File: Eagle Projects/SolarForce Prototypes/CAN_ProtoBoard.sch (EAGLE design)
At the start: 18 parts, among them U1 MCP2551

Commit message: CAN ProtoPCB V1 Ready..
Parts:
- added !INT, CLKOUT, RX, RX0BF, RX1BF, TX, TX0RTS, TX1RTS, TX2RTS, VBAT, VREF: (no value), pinhead:PINHD-1X1
- added C11: 100uF, resistor:CPOL-USD
- added C5, C6: 560pF, resistor:C-EUC0805K
- added CAN: (no value), pinhead:PINHD-1X4
- added CANSCREW: (no value), con-wago-500:W237-103
- added IO: (no value), pinhead:PINHD-1X10
- added JLINE, KLINE: (no value), pinhead:PINHD-1X3
- added R7: 120E, resistor:R-US_R0805
- added R8, R9: 100E, resistor:R-US_R0805
- added SJ1: Term, SparkFun-Retired:SOLDERJUMPERTRACE
- Q1: value (none) -> 16MHz
- R3, R4, R6: value (none) -> 1k
- renumbered JP1 to DB9M
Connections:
- new net CLKOUT: CLKOUT.1, U$1G$1.CLKOUT
- new net N$10: U1.VREF, VREF.1
- new net N$11: C5.2, R8.1
- new net N$12: C6.2, R9.1
- new net N$16: IO.3
- new net N$9: R7.1, SJ1.2
- new net RX0BF: RX0BF.1, U$1G$1.!RX0BF
- new net RX1BF: RX1BF.1, U$1G$1.!RX1BF
- new net TX0RTS: TX0RTS.1, U$1G$1.!TX0RTS
- new net TX1RTS: TX1RTS.1, U$1G$1.!TX1RTS
- new net TX2RTS: TX2RTS.1, U$1G$1.!TX2RTS
- net +5V: now also C11.+, CAN.4, IO.10, IO.2
- net CANH: now also CAN.3, CANSCREW-1.KL, R9.2, SJ1.1
- net CANL: now also CAN.2, CANSCREW-2.KL, R7.2, R8.2
- net CS: now also IO.8
- net GND: now also C11.-, C5.1, C6.1, CAN.1, CANSCREW-3.KL, IO.1, IO.9, JLINE.1, KLINE.1
- net INT: now also !INT.1, IO.4
- net J+: now also JLINE.3
- net J-: now also JLINE.2
- net K: now also KLINE.3
- net L: now also KLINE.2
- net RXCAN: now also RX.1
- net SCK: now also IO.5
- net SI: now also IO.6
- net SO: now also IO.7
- net TXCAN: now also TX.1
- net VBAT: now also VBAT.1

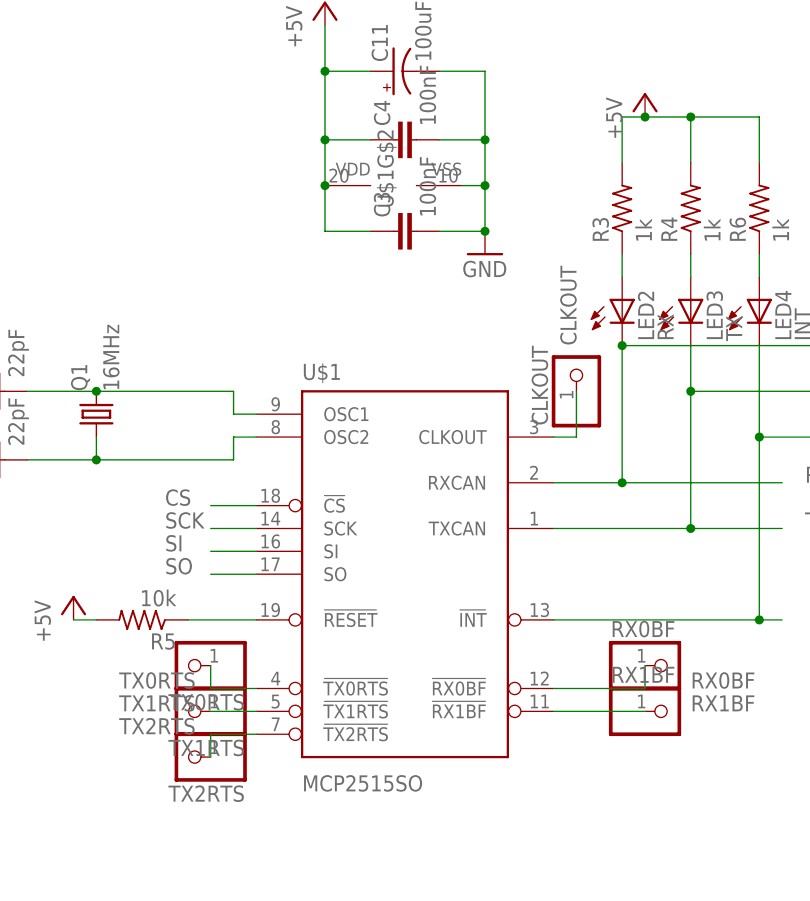
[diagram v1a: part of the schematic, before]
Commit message: Used wrong package for MCP2515.. SO not TSSOP!! Changed and fixxed...
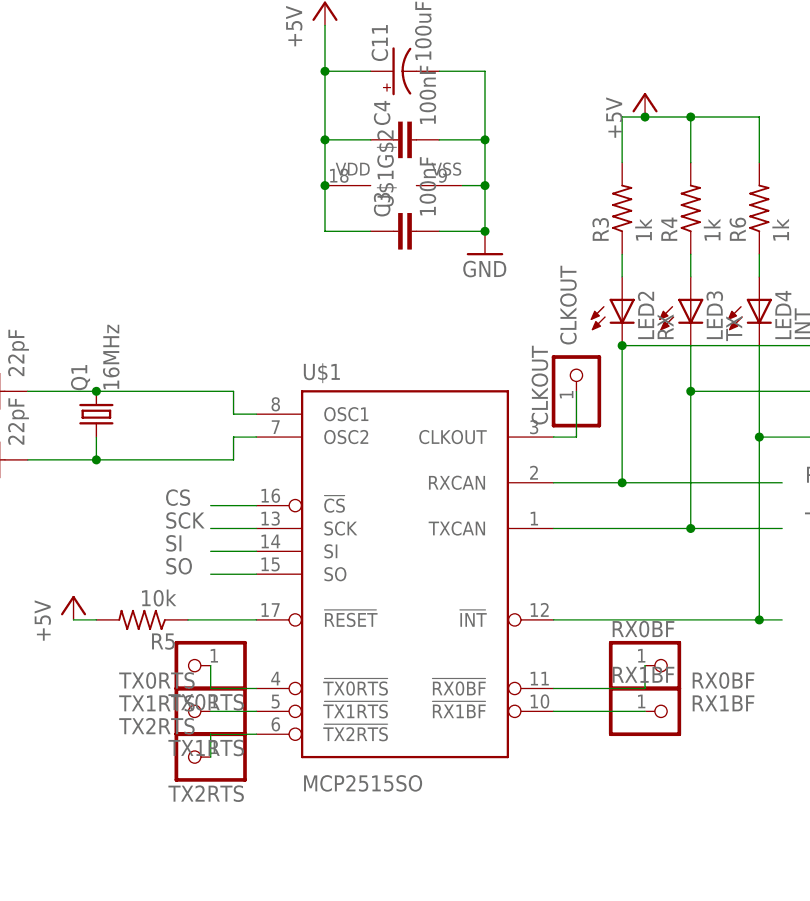
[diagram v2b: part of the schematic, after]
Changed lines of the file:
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@@
 <instances>
 <instance part="U1" gate="MCP2551" x="195.58" y="66.04"/>
-<instance part="U$1" gate="G$1" x="99.06" y="58.42"/>
 <instance part="Q1" gate="G$1" x="63.5" y="76.2" rot="R90"/>
 <instance part="U$1" gate="G$2" x="96.52" y="101.6" rot="R90"/>
@@
 <instance part="C11" gate="G$1" x="96.52" y="114.3" rot="R90"/>
 <instance part="VBAT" gate="G$1" x="309.88" y="63.5"/>
+<instance part="U$1" gate="G$1" x="99.06" y="58.42"/>
 </instances>
 <busses>
@@
 <net name="RXCAN" class="0">
 <segment>
-<pinref part="U$1" gate="G$1" pin="RXCAN"/>
 <wire x1="114.3" y1="68.58" x2="121.92" y2="68.58" width="0.1524" layer="91"/>
 <label x="142.24" y="68.58" size="1.778" layer="95"/>
@@
 <wire x1="147.32" y1="83.82" x2="121.92" y2="83.82" width="0.1524" layer="91"/>
 <junction x="121.92" y="83.82"/>
+<pinref part="U$1" gate="G$1" pin="RXCAN"/>
 </segment>
 <segment>
@@
 </segment>
 <segment>
-<pinref part="U$1" gate="G$1" pin="TXCAN"/>
 <wire x1="114.3" y1="63.5" x2="129.54" y2="63.5" width="0.1524" layer="91"/>
 <label x="142.24" y="63.5" size="1.778" layer="95"/>
@@
 <wire x1="147.32" y1="78.74" x2="129.54" y2="78.74" width="0.1524" layer="91"/>
 <junction x="129.54" y="78.74"/>
+<pinref part="U$1" gate="G$1" pin="TXCAN"/>
 </segment>
 </net>
@@
 <net name="N$1" class="0">
 <segment>
-<pinref part="U$1" gate="G$1" pin="OSC1"/>
 <wire x1="81.28" y1="76.2" x2="78.74" y2="76.2" width="0.1524" layer="91"/>
 <wire x1="78.74" y1="76.2" x2="78.74" y2="78.74" width="0.1524" layer="91"/>
@@
 <wire x1="63.5" y1="78.74" x2="55.88" y2="78.74" width="0.1524" layer="91"/>
 <junction x="63.5" y="78.74"/>
+<pinref part="U$1" gate="G$1" pin="OSC1"/>
 </segment>
 </net>
 <net name="N$2" class="0">
 <segment>
-<pinref part="U$1" gate="G$1" pin="OSC2"/>
 <wire x1="81.28" y1="73.66" x2="78.74" y2="73.66" width="0.1524" layer="91"/>
 <wire x1="78.74" y1="73.66" x2="78.74" y2="71.12" width="0.1524" layer="91"/>
@@
 <wire x1="63.5" y1="71.12" x2="55.88" y2="71.12" width="0.1524" layer="91"/>
 <junction x="63.5" y="71.12"/>
+<pinref part="U$1" gate="G$1" pin="OSC2"/>
 </segment>
 </net>
@@
 <net name="INT" class="0">
 <segment>
-<pinref part="U$1" gate="G$1" pin="!INT"/>
 <wire x1="114.3" y1="53.34" x2="137.16" y2="53.34" width="0.1524" layer="91"/>
 <label x="144.78" y="53.34" size="1.778" layer="95"/>
@@
 <wire x1="147.32" y1="73.66" x2="137.16" y2="73.66" width="0.1524" layer="91"/>
 <junction x="137.16" y="73.66"/>
+<pinref part="U$1" gate="G$1" pin="!INT"/>
 </segment>
 <segment>
@@
 <net name="N$5" class="0">
 <segment>
-<pinref part="U$1" gate="G$1" pin="!RESET"/>
 <pinref part="R5" gate="G$1" pin="1"/>
 <wire x1="81.28" y1="53.34" x2="73.66" y2="53.34" width="0.1524" layer="91"/>
+<pinref part="U$1" gate="G$1" pin="!RESET"/>
 </segment>
 </net>
@@
 <net name="CS" class="0">
 <segment>
-<pinref part="U$1" gate="G$1" pin="!CS"/>
 <wire x1="81.28" y1="66.04" x2="76.2" y2="66.04" width="0.1524" layer="91"/>
 <label x="71.12" y="66.04" size="1.778" layer="95"/>
+<pinref part="U$1" gate="G$1" pin="!CS"/>
 </segment>
 <segment>
@@
 <net name="SCK" class="0">
 <segment>
-<pinref part="U$1" gate="G$1" pin="SCK"/>
 <wire x1="81.28" y1="63.5" x2="76.2" y2="63.5" width="0.1524" layer="91"/>
 <label x="71.12" y="63.5" size="1.778" layer="95"/>
+<pinref part="U$1" gate="G$1" pin="SCK"/>
 </segment>
 <segment>
@@
 <net name="SI" class="0">
 <segment>
-<pinref part="U$1" gate="G$1" pin="SI"/>
 <wire x1="81.28" y1="60.96" x2="76.2" y2="60.96" width="0.1524" layer="91"/>
 <label x="71.12" y="60.96" size="1.778" layer="95"/>
+<pinref part="U$1" gate="G$1" pin="SI"/>
 </segment>
 <segment>
@@
 <net name="SO" class="0">
 <segment>
-<pinref part="U$1" gate="G$1" pin="SO"/>
 <wire x1="81.28" y1="58.42" x2="76.2" y2="58.42" width="0.1524" layer="91"/>
 <label x="71.12" y="58.42" size="1.778" layer="95"/>
+<pinref part="U$1" gate="G$1" pin="SO"/>
 </segment>
 <segment>
@@
 <net name="TX0RTS" class="0">
 <segment>
-<pinref part="U$1" gate="G$1" pin="!TX0RTS"/>
 <pinref part="TX0RTS" gate="G$1" pin="1"/>
 <wire x1="81.28" y1="45.72" x2="76.2" y2="45.72" width="0.1524" layer="91"/>
 <wire x1="76.2" y1="45.72" x2="76.2" y2="48.26" width="0.1524" layer="91"/>
 <label x="66.04" y="45.72" size="1.778" layer="95"/>
+<pinref part="U$1" gate="G$1" pin="!TX0RTS"/>
 </segment>
 </net>
 <net name="TX1RTS" class="0">
 <segment>
-<pinref part="U$1" gate="G$1" pin="!TX1RTS"/>
 <pinref part="TX1RTS" gate="G$1" pin="1"/>
 <wire x1="81.28" y1="43.18" x2="76.2" y2="43.18" width="0.1524" layer="91"/>
 <label x="66.04" y="43.18" size="1.778" layer="95"/>
+<pinref part="U$1" gate="G$1" pin="!TX1RTS"/>
 </segment>
 </net>
 <net name="TX2RTS" class="0">
 <segment>
-<pinref part="U$1" gate="G$1" pin="!TX2RTS"/>
 <pinref part="TX2RTS" gate="G$1" pin="1"/>
 <wire x1="81.28" y1="40.64" x2="76.2" y2="40.64" width="0.1524" layer="91"/>
 <wire x1="76.2" y1="40.64" x2="76.2" y2="38.1" width="0.1524" layer="91"/>
 <label x="66.04" y="40.64" size="1.778" layer="95"/>
+<pinref part="U$1" gate="G$1" pin="!TX2RTS"/>
 </segment>
 </net>
 <net name="RX0BF" class="0">
 <segment>
-<pinref part="U$1" gate="G$1" pin="!RX0BF"/>
 <pinref part="RX0BF" gate="G$1" pin="1"/>
 <wire x1="114.3" y1="45.72" x2="124.46" y2="45.72" width="0.1524" layer="91"/>
 <wire x1="124.46" y1="45.72" x2="124.46" y2="48.26" width="0.1524" layer="91"/>
 <label x="129.54" y="45.72" size="1.778" layer="95"/>
+<pinref part="U$1" gate="G$1" pin="!RX0BF"/>
 </segment>
 </net>
 <net name="RX1BF" class="0">
 <segment>
-<pinref part="U$1" gate="G$1" pin="!RX1BF"/>
 <pinref part="RX1BF" gate="G$1" pin="1"/>
 <wire x1="114.3" y1="43.18" x2="124.46" y2="43.18" width="0.1524" layer="91"/>
 <label x="129.54" y="43.18" size="1.778" layer="95"/>
+<pinref part="U$1" gate="G$1" pin="!RX1BF"/>
 </segment>
 </net>
 <net name="CLKOUT" class="0">
 <segment>
-<pinref part="U$1" gate="G$1" pin="CLKOUT"/>
 <pinref part="CLKOUT" gate="G$1" pin="1"/>
 <wire x1="114.3" y1="73.66" x2="116.84" y2="73.66" width="0.1524" layer="91"/>
 <wire x1="116.84" y1="73.66" x2="116.84" y2="78.74" width="0.1524" layer="91"/>
 <label x="116.84" y="83.82" size="1.778" layer="95" rot="R90"/>
-</segment>
-</net>
+<pinref part="U$1" gate="G$1" pin="CLKOUT"/>
+</segment>
+</net>
